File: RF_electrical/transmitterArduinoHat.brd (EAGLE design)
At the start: 100 x 74.9 mm, 21 parts

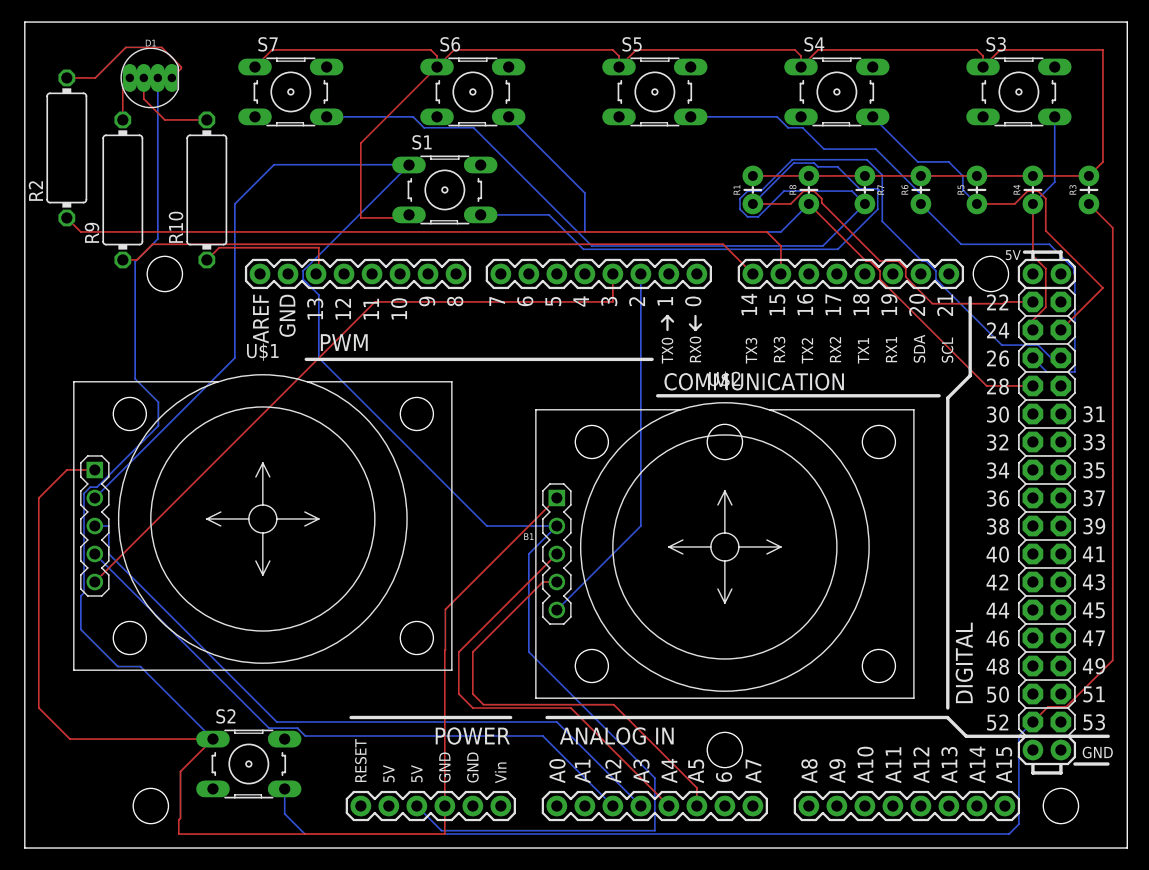
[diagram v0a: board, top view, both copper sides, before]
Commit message: Added RF device to schematic & PCB. Starting to create prototype cpp program on Arduino.
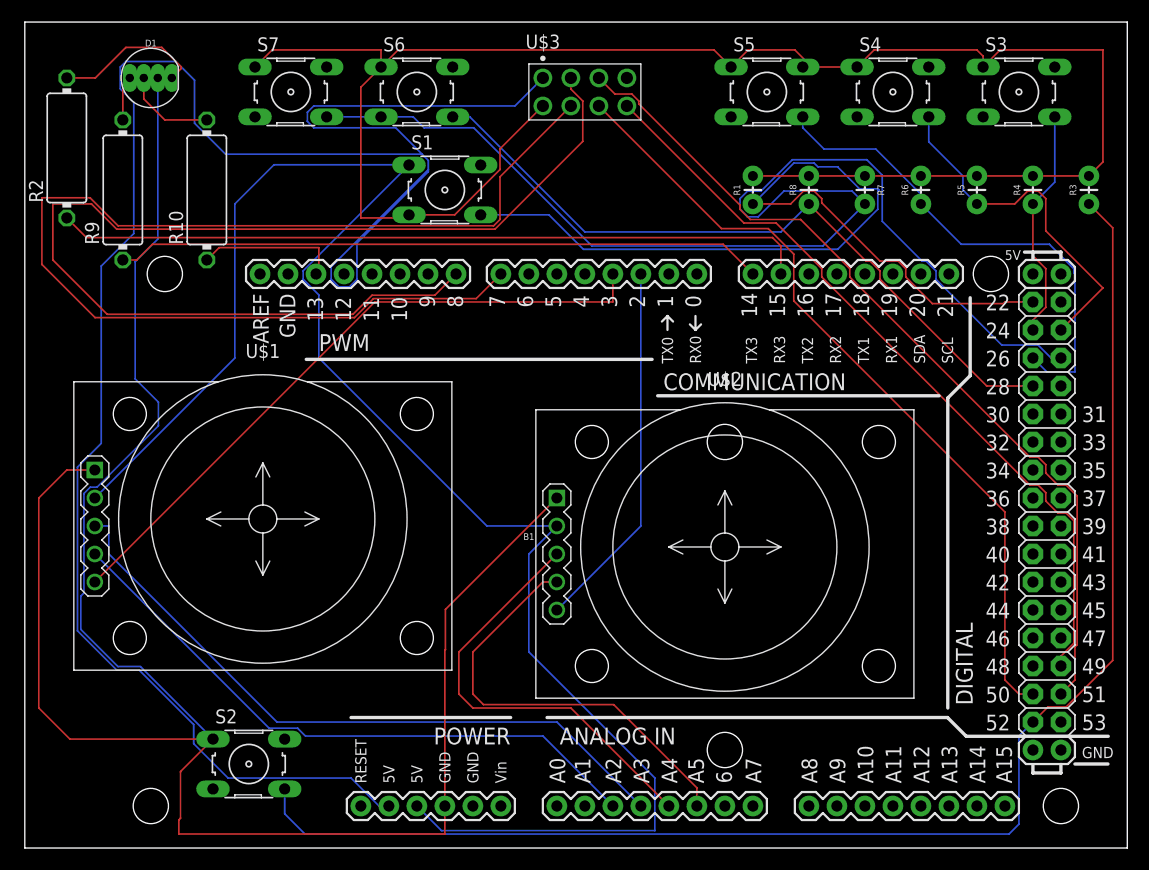
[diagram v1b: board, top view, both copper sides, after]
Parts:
- added U$3: AS01-ML01DP5_DEVICEPIN_HEADS, diy01-arduino-library:HDRV8W64P254_2X4_1016X508X838B
- moved S5 10.2 mm to (67.3, 68.6)
- moved S4 5.08 mm to (78.7, 68.6)
- moved S6 5.08 mm to (35.6, 68.6)
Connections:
- new net N$14: B1.3.3V, U$3.1
- new net N$21: B1.8, U$3.2
- new net N$22: B1.7, U$3.7
- new net N$23: B1.51, U$3.3
- new net N$24: B1.50, U$3.6
- new net N$25: B1.49, U$3.5
- net GND: now also U$3.8
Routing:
- net N$14: track 0.00 -> 188.8 mm
- net N$22: track 0.00 -> 107.1 mm
- net N$21: track 0.00 -> 103.7 mm
- net N$23: track 0.00 -> 78.9 mm
- net N$24: track 0.00 -> 72.9 mm
- net N$25: track 0.00 -> 70.7 mm
- net GND: track 330.5 -> 344.9 mm
- net N$10: track 54.7 -> 45.1 mm
- net N$7: track 36.1 -> 32.4 mm
- net N$13: track 62.3 -> 65.3 mm

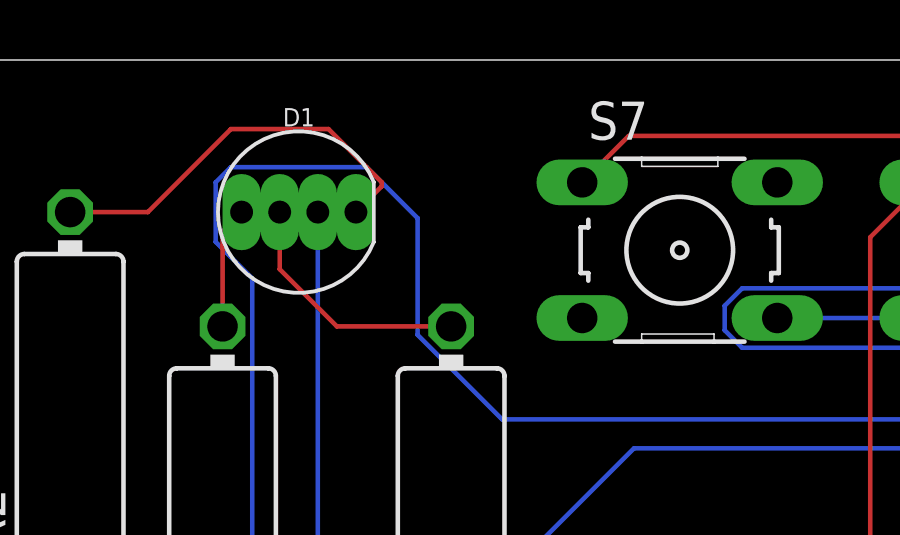
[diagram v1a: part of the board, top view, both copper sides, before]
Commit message: Fixed GND connection in PCB. Revised code, ready for LED testing once PCB is ready.
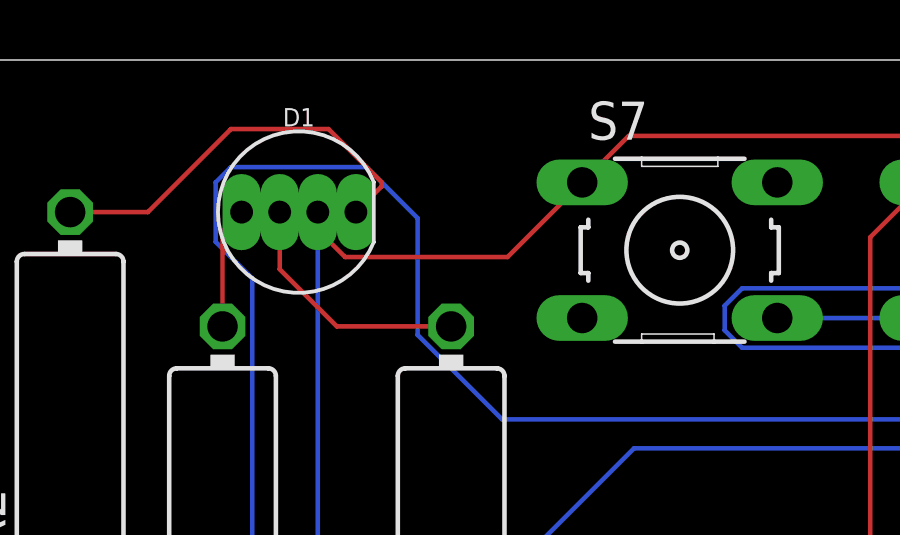
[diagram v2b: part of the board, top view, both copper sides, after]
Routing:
- net GND: track 344.9 -> 355.7 mm
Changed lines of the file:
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@@
 </layers>
 <board>
-<fusionsync huburn="a.YnVzaW5lc3M6Z21haWw5OTA1NzM" projecturn="a.YnVzaW5lc3M6Z21haWw5OTA1NzMjRDIwMjAwNjI2MzExMTM2MzU2" f3durn="urn:adsk.wipprod:dm.lineage:T7YeBB7jRpiTvm4awXTaew" pcbguid="" lastpulledtime="" lastsyncedchangeguid="" latestrevisionid="89036a89-cee6-4bfb-a609-c29f545d92eb" lastsyncedrevisionid="89036a89-cee6-4bfb-a609-c29f545d92eb" lastboardhashguid="a2a36bed-28bb-8ddf-2adb-c959e81b010c" lastpushedtime="2020-06-26T20:15:32Z" linktopcb3d="true"/>
+<fusionsync huburn="a.YnVzaW5lc3M6Z21haWw5OTA1NzM" projecturn="a.YnVzaW5lc3M6Z21haWw5OTA1NzMjRDIwMjAwNjI2MzExMTM2MzU2" f3durn="urn:adsk.wipprod:dm.lineage:T7YeBB7jRpiTvm4awXTaew" pcbguid="" lastpulledtime="" lastsyncedchangeguid="" latestrevisionid="89036a89-cee6-4bfb-a609-c29f545d92eb" lastsyncedrevisionid="89036a89-cee6-4bfb-a609-c29f545d92eb" lastboardhashguid="a2a36bed-28bb-8ddf-2adb-c959e81b010c" lastpushedtime="2020-06-26T20:15:32Z" linktopcb3d="false"/>
 <plain>
 <wire x1="0" y1="0" x2="100" y2="0" width="0" layer="20"/>
@@
 <wire x1="43.1038" y1="61.540275" x2="38.992925" y2="57.4294" width="0.1524" layer="1"/>
 <wire x1="38.992925" y1="57.4294" x2="34.8488" y2="57.4294" width="0.1524" layer="1"/>
+<wire x1="12.4714" y1="68.85728125" x2="12.97728125" y2="68.3514" width="0.1524" layer="1"/>
+<wire x1="12.065" y1="69.85" x2="12.4714" y2="69.4436" width="0.1524" layer="1"/>
+<wire x1="12.4714" y1="69.4436" x2="12.4714" y2="68.85728125" width="0.1524" layer="1"/>
+<wire x1="12.97728125" y1="68.3514" x2="18.3896" y2="68.3514" width="0.1524" layer="1"/>
+<wire x1="18.3896" y1="68.3514" x2="20.8788" y2="70.8406" width="0.1524" layer="1"/>
 <wire x1="71.12" y1="60.96" x2="76.2" y2="60.96" width="0" layer="19" extent="1-1"/>
 <wire x1="81.28" y1="60.96" x2="76.2" y2="60.96" width="0" layer="19" extent="1-1"/>
-<wire x1="12.065" y1="69.85" x2="20.8788" y2="70.8406" width="0" layer="19" extent="1-1"/>
 </signal>
 <signal name="+5V">
